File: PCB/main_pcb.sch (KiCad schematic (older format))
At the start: 15 parts, among them P1 SEN, P2 SRV, P3 PWR, P4 LED, P5 M1, P6 M2, Q1 5LN01SP, U1 Teensy_3.1, U2 RFM69_Breakout, U5 DRV8834_Breakout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

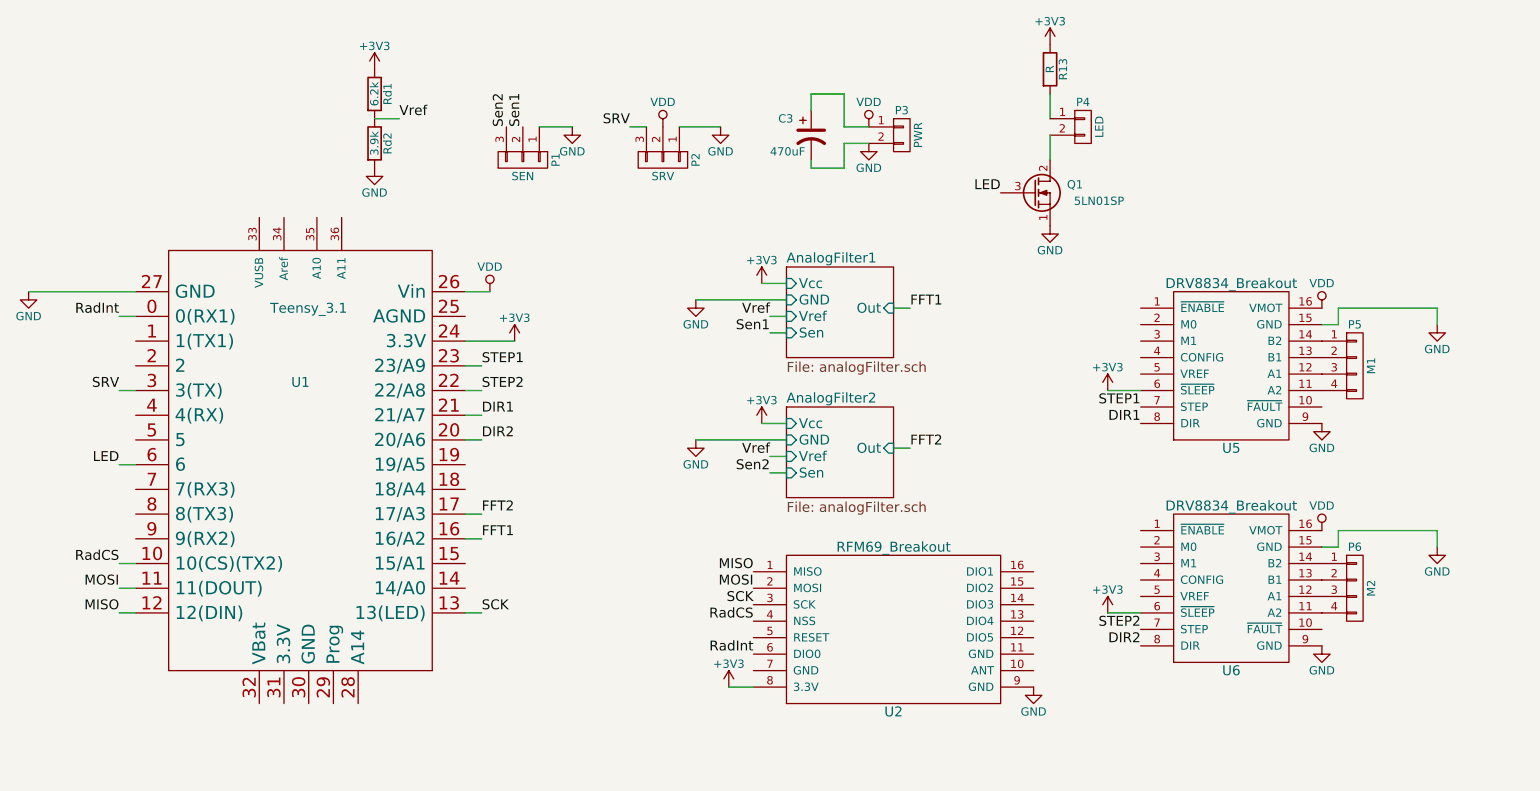
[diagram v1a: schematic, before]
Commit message: Improved simulation, did most of the pcb trace layout
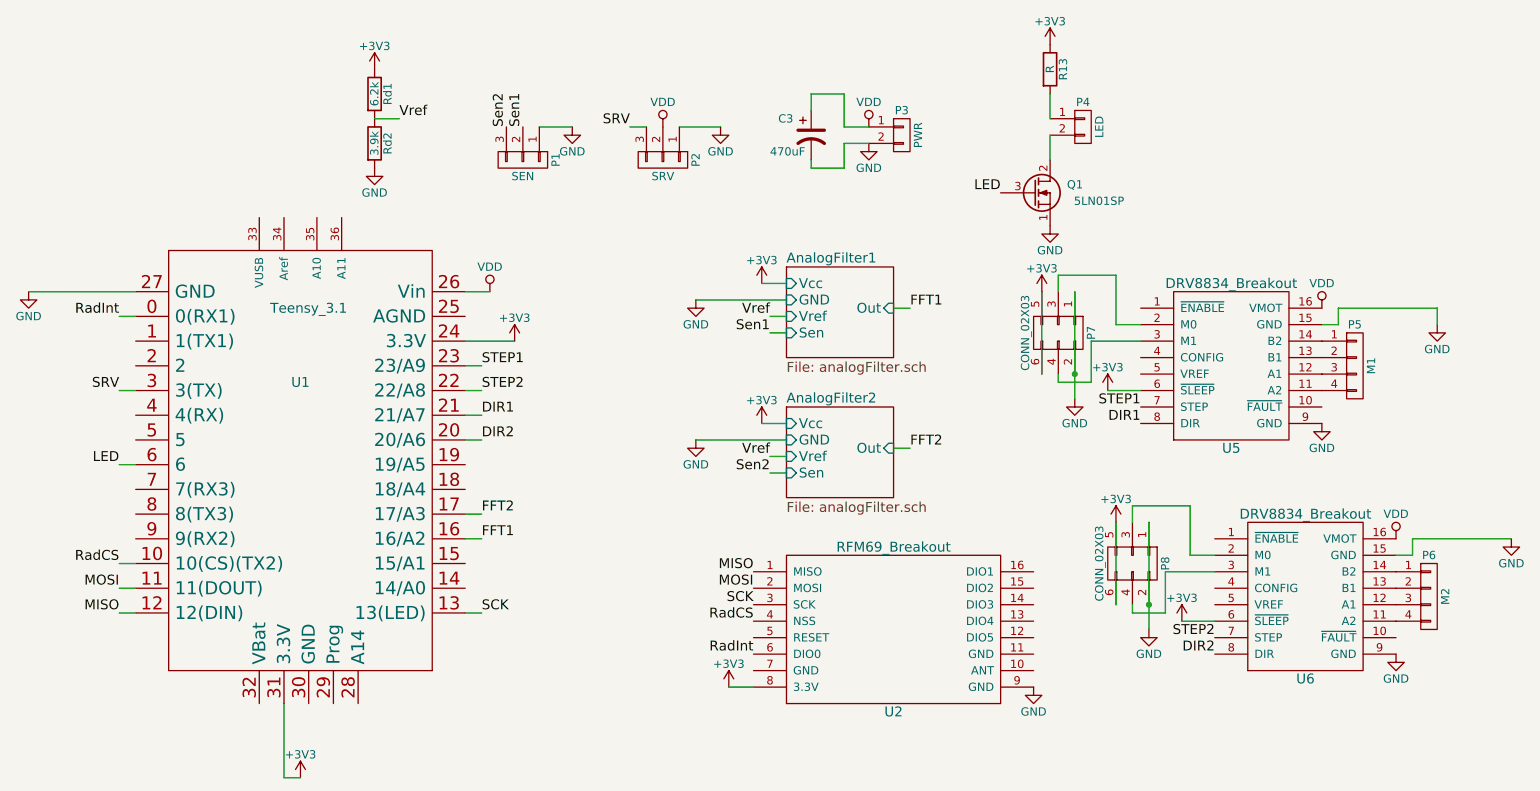
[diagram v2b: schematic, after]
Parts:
- added P7, P8: CONN_02X03, Pin_Headers:Pin_Header_Straight_2x03_Pitch2.54mm, symbol CONN_02X03
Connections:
- net +3V3: now also U1.31 (3.3V), P7.5 (P5), P7.6 (P6), P8.5 (P5), P8.6 (P6)
- net GND: now also P7.1 (P1), P7.2 (P2), P8.1 (P1), P8.2 (P2)
- net at U5.2 (M0): now also P7.3 (P3)
- net at U5.3 (M1): now also P7.4 (P4)
- net at U6.2 (M0): now also P8.3 (P3)
- net at U6.3 (M1): now also P8.4 (P4)
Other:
- moved on the sheet: P6, U6

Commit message: Finished PCB and robot designs
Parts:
- Rd2: value 3.9k -> 1.5k
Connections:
- net GND: now also U2.11 (GND)
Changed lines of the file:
@@
 P 3400 2250
 F 0 "Rd2" V 3480 2250 50  0000 C CNN
-F 1 "3.9k" V 3400 2250 50  0000 C CNN
+F 1 "1.5k" V 3400 2250 50  0000 C CNN
 F 2 "Resistors_ThroughHole:R_Axial_DIN0207_L6.3mm_D2.5mm_P7.62mm_Horizontal" V 3330 2250 50  0001 C CNN
 F 3 "" H 3400 2250 50  0000 C CNN
@@
 Wire Wire Line
 	2850 6100 2850 5650
+$Comp
+L GND #PWR?
+U 1 1 594A8840
+P 7550 5350
+F 0 "#PWR?" H 7550 5100 50  0001 C CNN
+F 1 "GND" H 7550 5200 50  0000 C CNN
+F 2 "" H 7550 5350 50  0000 C CNN
+F 3 "" H 7550 5350 50  0000 C CNN
+	1    7550 5350
+	1    0    0    -1
+$EndComp
+Wire Wire Line
+	7400 5350 7550 5350
 $EndSCHEMATC

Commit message: minor pcb and BOM adjustments
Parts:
- R13: value R -> 10R
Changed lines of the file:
@@
 P 7500 1800
 F 0 "R13" V 7580 1800 50  0000 C CNN
-F 1 "R" V 7500 1800 50  0000 C CNN
+F 1 "10R" V 7500 1800 50  0000 C CNN
 F 2 "Resistors_ThroughHole:R_Axial_DIN0207_L6.3mm_D2.5mm_P7.62mm_Horizontal" V 7430 1800 50  0001 C CNN
 F 3 "" H 7500 1800 50  0000 C CNN
@@
 	2850 6100 2850 5650
 $Comp
-L GND #PWR?
+L GND #PWR032
 U 1 1 594A8840
 P 7550 5350
-F 0 "#PWR?" H 7550 5100 50  0001 C CNN
+F 0 "#PWR032" H 7550 5100 50  0001 C CNN
 F 1 "GND" H 7550 5200 50  0000 C CNN
 F 2 "" H 7550 5350 50  0000 C CNN

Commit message: pcb revisions
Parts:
- added P9: Range, Pin_Headers:Pin_Header_Straight_2x01_Pitch2.54mm, symbol CONN_01X02
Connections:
- net GND: now also P3.1 (P1); no longer P3.2 (P2)
- net RadInt: now also U2.15 (DIO2); no longer U2.6 (DIO0)
- net VDD: now also P3.2 (P2); no longer P3.1 (P1)
- net Reset: now reaches U1.1 (1(TX1))
- net Reset: now also U2.5 (RESET)
- net at U1.18 (18/A4): now also P9.1 (P1)
- net at U1.19 (19/A5): now also P9.2 (P2)
- net at Q1.2 (D): now also P4.1 (P1); no longer P4.2 (P2)
- net at R13.2: now also P4.2 (P2); no longer P4.1 (P1)
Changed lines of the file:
@@
 F 3 "" H 6600 2200 50  0000 C CNN
 	1    6600 2200
-	1    0    0    -1
+	1    0    0    1
 $EndComp
 $Comp
@@
 Text Label 5700 5150 2    60   ~ 0
 RadCS
-Text Label 5700 5350 2    60   ~ 0
+Text Label 7550 4750 2    60   ~ 0
 RadInt
 Text Label 1850 5100 2    60   ~ 0
@@
 F 3 "" H 7700 2150 50  0000 C CNN
 	1    7700 2150
-	1    0    0    -1
+	1    0    0    1
 $EndComp
 $Comp
@@
 Wire Wire Line
 	7400 5350 7550 5350
+Wire Wire Line
+	7550 4750 7550 4950
+Wire Wire Line
+	7550 4950 7400 4950
+Text Label 1850 3450 2    60   ~ 0
+Reset
+Wire Wire Line
+	1850 3450 1950 3450
+Text Label 5700 5250 2    60   ~ 0
+Reset
+$Comp
+L CONN_01X02 P9
+U 1 1 5966E4C1
+P 4600 4250
+F 0 "P9" H 4600 4400 50  0000 C CNN
+F 1 "Range" V 4700 4250 50  0000 C CNN
+F 2 "Pin_Headers:Pin_Header_Straight_2x01_Pitch2.54mm" H 4600 4250 50  0001 C CNN
+F 3 "" H 4600 4250 50  0000 C CNN
+	1    4600 4250
+	1    0    0    1
+$EndComp
+Wire Wire Line
+	4400 4200 3950 4200
+Wire Wire Line
+	3950 4350 4400 4350
+Wire Wire Line
+	4400 4350 4400 4300
 $EndSCHEMATC
